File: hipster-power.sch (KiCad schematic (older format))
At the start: 14 parts, among them Q201 FDN340P, SW201 ON|OFF, U201 MCP73831, U202 NCP5501

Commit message: Updated to use new switch.
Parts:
- SW201: footprint libs:SS12D00 -> libs:SK12D07VG5
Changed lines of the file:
@@
 F 0 "SW201" H 2850 4450 50  0000 C CNN
 F 1 "ON|OFF" H 2850 4250 50  0000 C CNN
-F 2 "libs:SS12D00" H 2850 4350 50  0001 C CNN
+F 2 "libs:SK12D07VG5" H 2850 4350 50  0001 C CNN
 F 3 "" H 2850 4350 50  0000 C CNN
 	1    2850 4350

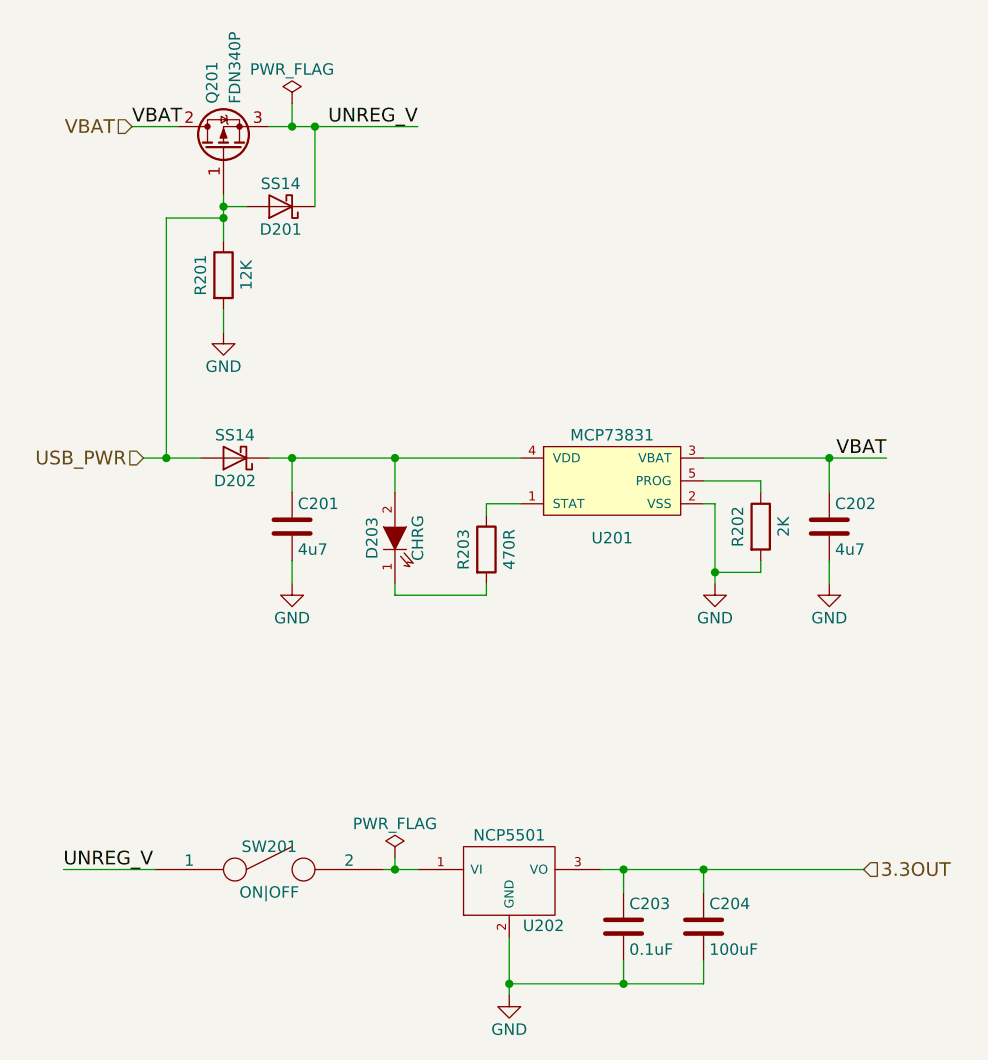
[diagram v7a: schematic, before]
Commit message: Add SZLCSC part links
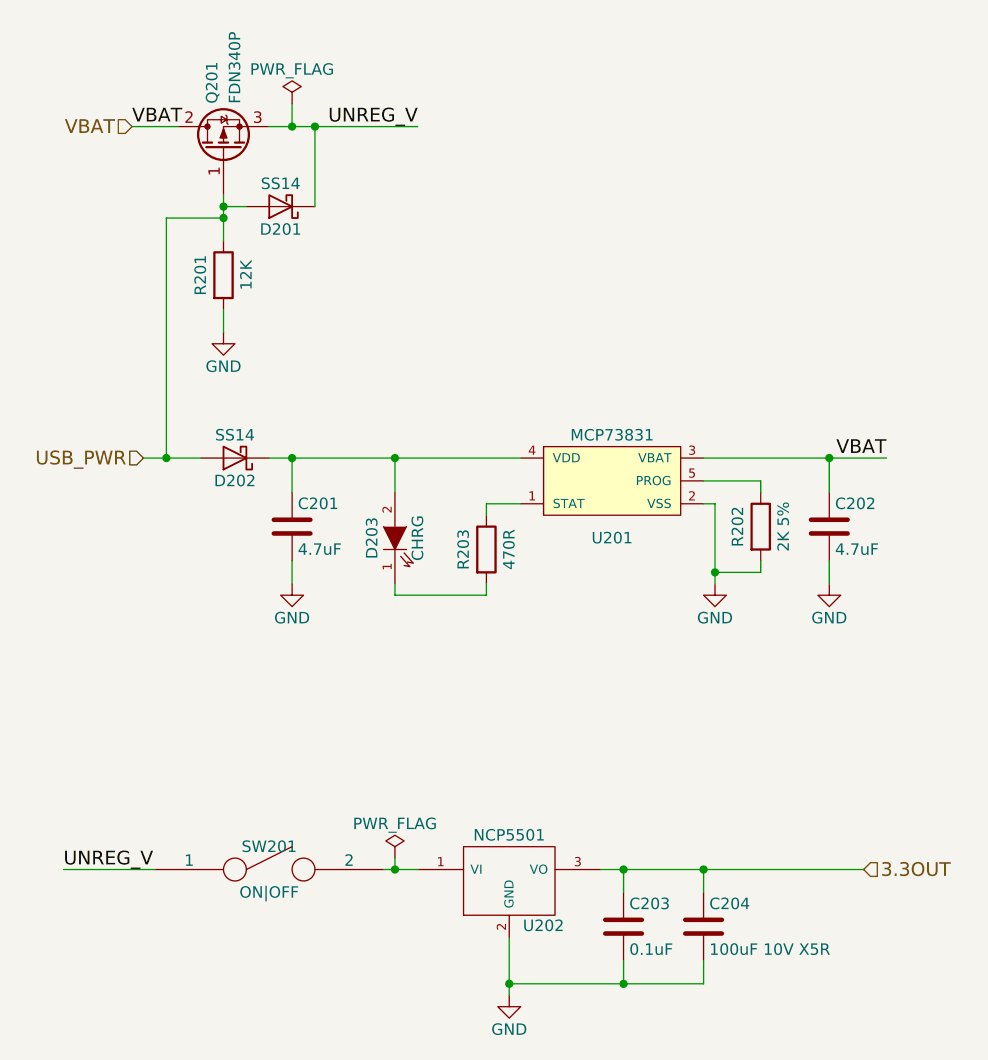
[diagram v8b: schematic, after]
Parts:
- C201, C202: value 4u7 -> 4.7uF; LCSC (none) -> http://www.szlcsc.com/product/details_99401.html
- C203: LCSC (none) -> http://www.szlcsc.com/product/details_2040.html
- C204: value 100uF -> 100uF 10V X5R; LCSC (none) -> http://www.szlcsc.com/product/details_24478.html
- D201, D202: LCSC (none) -> http://www.szlcsc.com/product/details_85512.html
- D203: LCSC (none) -> http://www.szlcsc.com/product/details_85432.html
- Q201: LCSC (none) -> http://www.szlcsc.com/product/details_87950.html
- R201: LCSC (none) -> http://www.szlcsc.com/product/details_101951.html
- R202: value 2K -> 2K 5%; LCSC (none) -> http://www.szlcsc.com/product/details_26333.html
- R203: LCSC (none) -> http://www.szlcsc.com/product/details_25984.html
- SW201: LCSC (none) -> http://www.szlcsc.com/product/details_39247.html
- U201: LCSC (none) -> http://www.szlcsc.com/product/details_15551.html
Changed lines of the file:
@@
 F 2 "Resistors_SMD:R_0603_HandSoldering" V 3730 2950 50  0001 C CNN
 F 3 "" H 3800 2950 50  0000 C CNN
+F 4 "http://www.szlcsc.com/product/details_25984.html" H 7350 2250 60  0001 C CNN "LCSC"
 	1    3800 2950
 	1    0    0    -1
@@
 F 2 "LEDs:LED_0603" H 3400 2900 50  0001 C CNN
 F 3 "" H 3400 2900 50  0000 C CNN
+F 4 "http://www.szlcsc.com/product/details_85432.html" H 7350 2250 60  0001 C CNN "LCSC"
 	1    3400 2900
 	0    -1   -1   0
@@
 P 2950 2850
 F 0 "C201" H 2975 2950 50  0000 L CNN
-F 1 "4u7" H 2975 2750 50  0000 L CNN
+F 1 "4.7uF" H 2975 2750 50  0000 L CNN
 F 2 "Capacitors_SMD:C_0805_HandSoldering" H 2988 2700 50  0001 C CNN
 F 3 "" H 2950 2850 50  0000 C CNN
+F 4 "http://www.szlcsc.com/product/details_99401.html" H 7350 2250 60  0001 C CNN "LCSC"
 	1    2950 2850
 	1    0    0    -1
@@
 P 5000 2850
 F 0 "R202" V 4900 2850 50  0000 C CNN
-F 1 "2K" V 5100 2850 50  0000 C CNN
+F 1 "2K 5%" V 5100 2850 50  0000 C CNN
 F 2 "Resistors_SMD:R_0603_HandSoldering" V 4930 2850 50  0001 C CNN
 F 3 "" H 5000 2850 50  0000 C CNN
+F 4 "http://www.szlcsc.com/product/details_26333.html" H 7350 2250 60  0001 C CNN "LCSC"
 	1    5000 2850
 	1    0    0    -1
@@
 F 2 "libs:SK12D07VG5" H 2850 4350 50  0001 C CNN
 F 3 "" H 2850 4350 50  0000 C CNN
+F 4 "http://www.szlcsc.com/product/details_39247.html" H 7350 2250 60  0001 C CNN "LCSC"
 	1    2850 4350
 	1    0    0    -1
@@
 F 6 "CC0603KRX7R7BB104" H 4400 4600 60  0001 C CNN "Manufactur PN"
 F 7 "0.10" H 4400 4600 60  0001 C CNN "Unit Cost"
+F 8 "http://www.szlcsc.com/product/details_2040.html" H 7350 2250 60  0001 C CNN "LCSC"
 	1    4400 4600
 	1    0    0    -1
@@
 P 4750 4600
 F 0 "C204" H 4775 4700 50  0000 L CNN
-F 1 "100uF" H 4775 4500 50  0000 L CNN
+F 1 "100uF 10V X5R" H 4775 4500 50  0000 L CNN
 F 2 "Capacitors_SMD:C_1210_HandSoldering" H 4788 4450 50  0001 C CNN
 F 3 "" H 4750 4600 50  0000 C CNN
@@
 F 6 "GRM31CR60J107ME39K" H 4750 4600 60  0001 C CNN "Manufacturer PN"
 F 7 "0.60" H 4750 4600 60  0001 C CNN "Unit Cost"
+F 8 "http://www.szlcsc.com/product/details_24478.html" H 7350 2250 60  0001 C CNN "LCSC"
 	1    4750 4600
 	1    0    0    -1
@@
 F 2 "TO_SOT_Packages_SMD:SOT-23-5_HandSoldering" H 4350 2650 60  0001 C CNN
 F 3 "" H 4350 2650 60  0000 C CNN
+F 4 "http://www.szlcsc.com/product/details_15551.html" H 7350 2250 60  0001 C CNN "LCSC"
 	1    4350 2650
 	1    0    0    -1
@@
 P 5300 2850
 F 0 "C202" H 5325 2950 50  0000 L CNN
-F 1 "4u7" H 5325 2750 50  0000 L CNN
+F 1 "4.7uF" H 5325 2750 50  0000 L CNN
 F 2 "Capacitors_SMD:C_0805_HandSoldering" H 5338 2700 50  0001 C CNN
 F 3 "" H 5300 2850 50  0000 C CNN
+F 4 "http://www.szlcsc.com/product/details_99401.html" H 7350 2250 60  0001 C CNN "LCSC"
 	1    5300 2850
 	1    0    0    -1
@@
 F 2 "Diodes_SMD:D_SMA" H 2900 1450 50  0001 C CNN
 F 3 "" H 2900 1450 50  0000 C CNN
+F 4 "http://www.szlcsc.com/product/details_85512.html" H 7350 2250 60  0001 C CNN "LCSC"
 	1    2900 1450
 	-1   0    0    1
@@
 F 2 "Resistors_SMD:R_0603_HandSoldering" V 2580 1750 50  0001 C CNN
 F 3 "" H 2650 1750 50  0000 C CNN
+F 4 "http://www.szlcsc.com/product/details_101951.html" H 7350 2250 60  0001 C CNN "LCSC"
 	1    2650 1750
 	1    0    0    -1
@@
 F 2 "Diodes_SMD:D_SMA" H 2700 2550 50  0001 C CNN
 F 3 "" H 2700 2550 50  0000 C CNN
+F 4 "http://www.szlcsc.com/product/details_85512.html" H 7350 2250 60  0001 C CNN "LCSC"
 	1    2700 2550
 	-1   0    0    1
@@
 F 2 "libs:SOT23_FET" H 2850 1300 50  0001 C CNN
 F 3 "" H 2650 1200 50  0001 C CNN
+F 4 "http://www.szlcsc.com/product/details_87950.html" H 7350 2250 60  0001 C CNN "LCSC"
 	1    2650 1200
 	0    -1   -1   0
